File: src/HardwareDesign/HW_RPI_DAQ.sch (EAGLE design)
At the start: 348 parts, among them IC10 ADS9234RIRHBR, IC11 MCP6001RT, IC12 MCP1525T-I/TT, IC13 MCP6001RT, IC14 TPS65131, IC15 TPS7A39, IC16 SN74LVC2G66, IC17 74LVC1G04, IC2 AP22653W6, IC22 DAC8568, IC23 MCP6001RT, IC24 MCP6001RT, IC25 MCP6001RT, IC26 MCP6001RT, IC27 MCP6001RT, IC28 MCP6001RT, IC29 MCP6001RT, IC3 74LVC1G07, IC30 MCP6001RT, IC31 MCP6001RT, IC32 LSF0108, IC33 LSF0108, IC34 LSF0108, IC35 LSF0108, IC36 MCP23S18, IC38 SN74LVC2G66, IC39 74LVC1G04, IC4 RT9742NGV, IC6 DG409, IC7 ADA4254ACPZ, IC8 DG409, IC9 ADA4254ACPZ, J1 10164227-1001A1RLF, J2 10164227-1001A1RLF, J7 2-5174225-5, SW1 1825027-8, T2 IRLML5203, X2 CRYSTAL

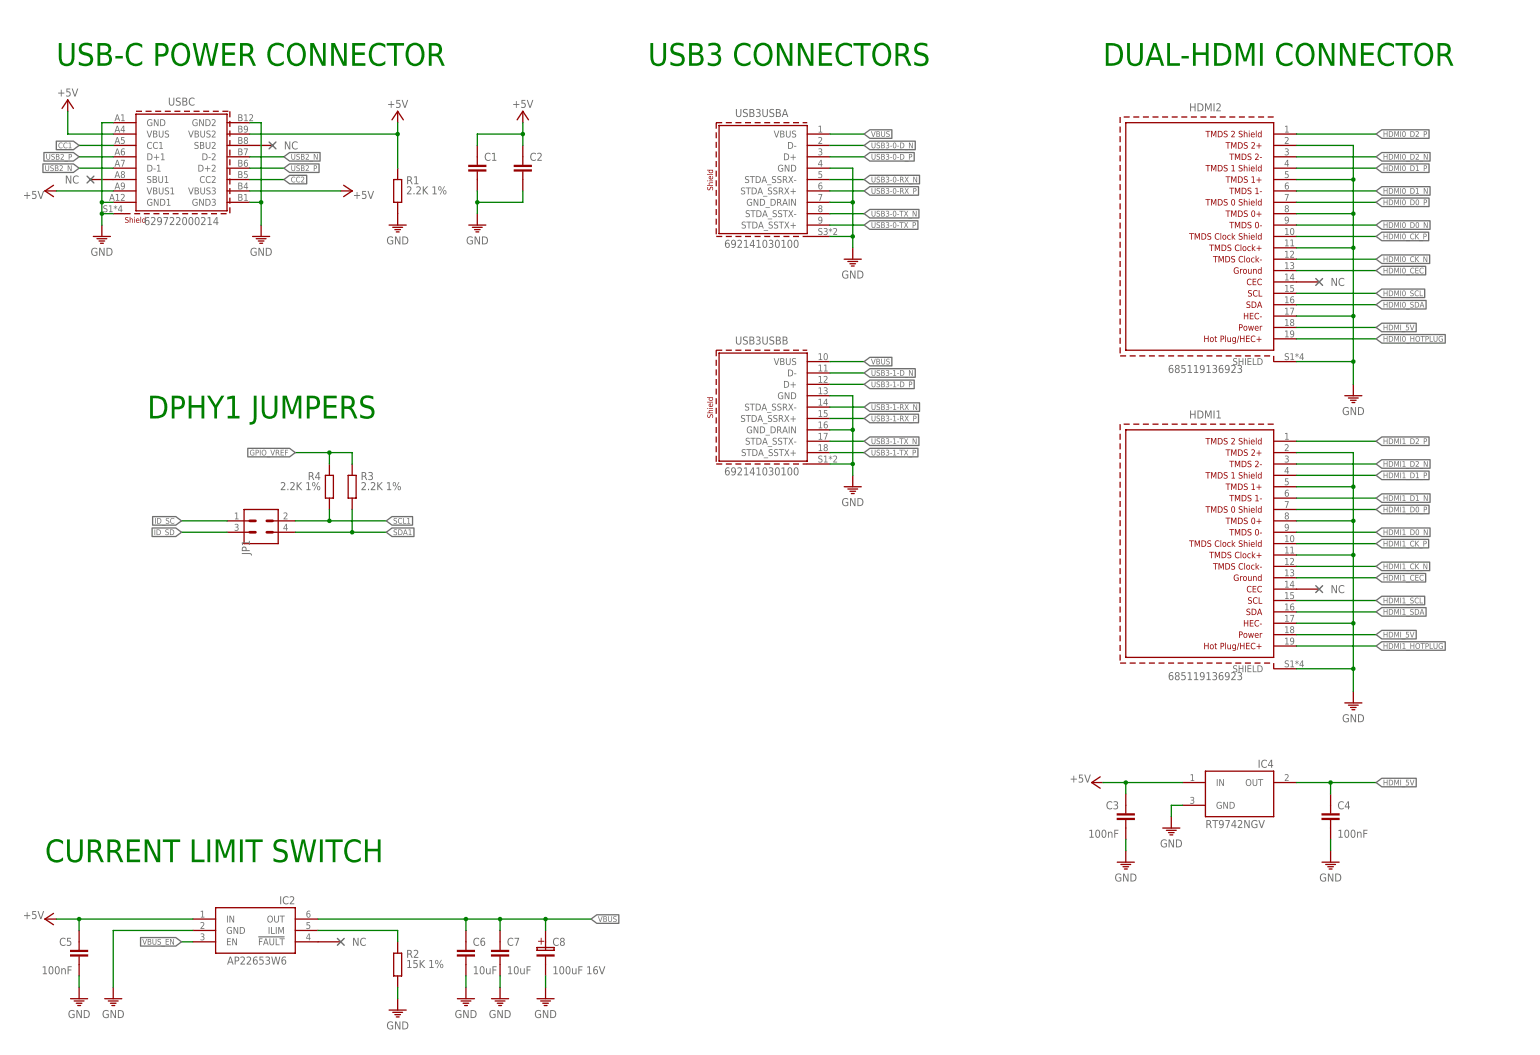
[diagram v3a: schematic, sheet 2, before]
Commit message: update schematics with new testpoints
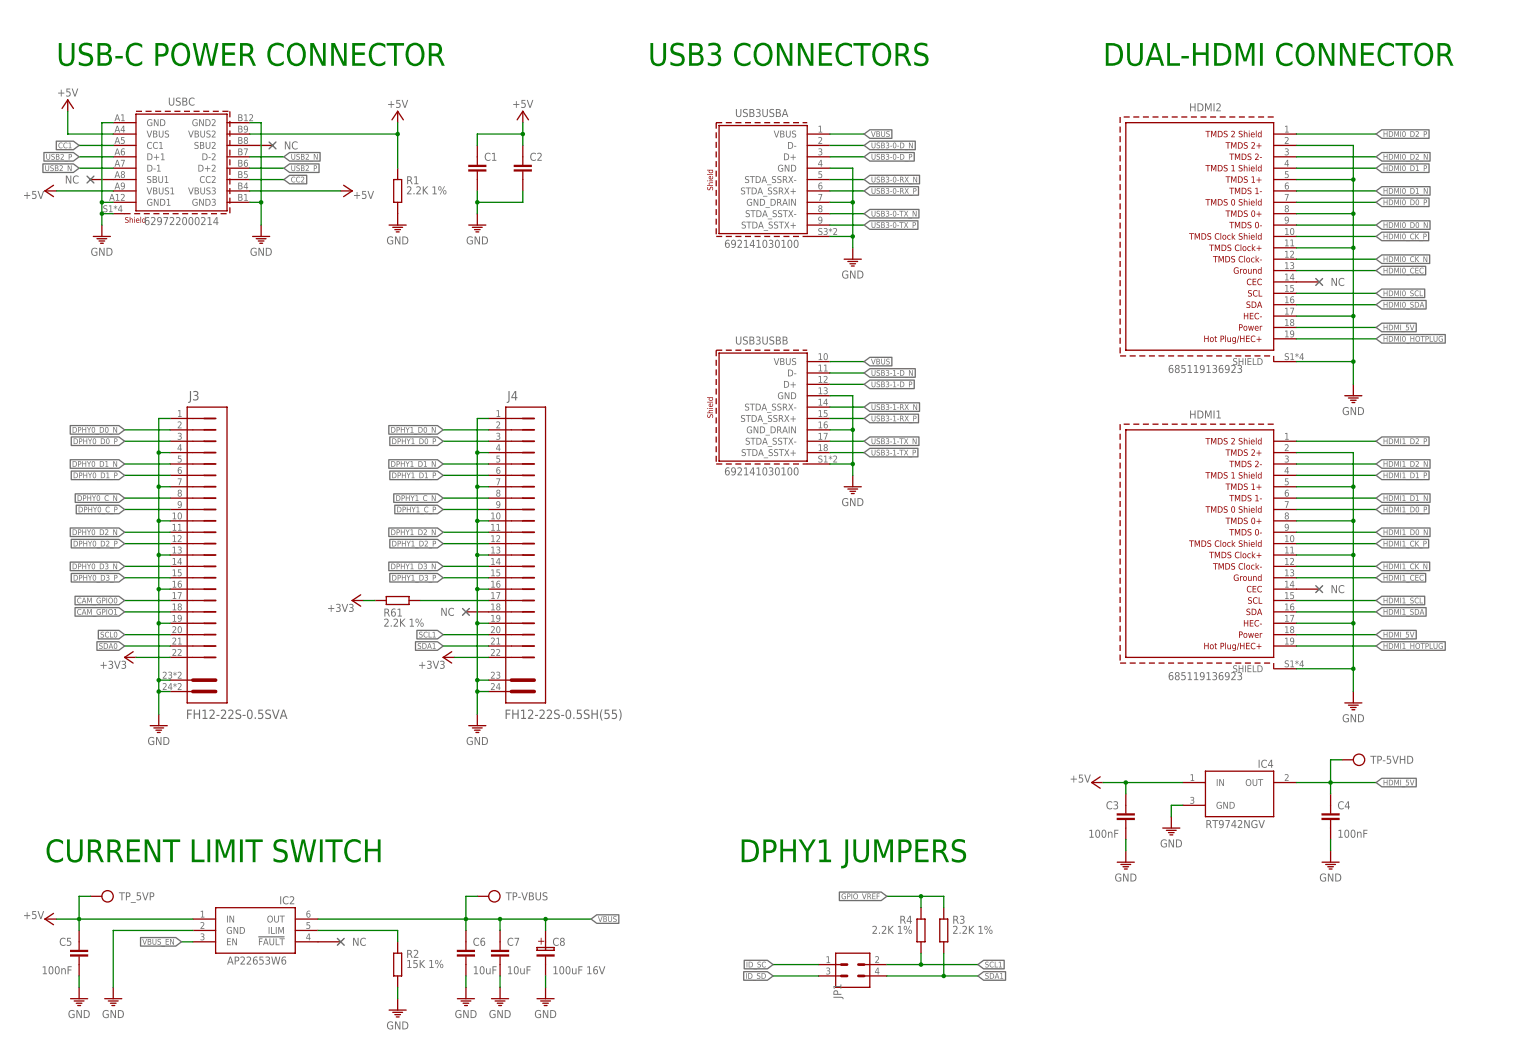
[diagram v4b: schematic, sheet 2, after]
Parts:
- added J3: FH12-22S-0.5SVA, ds_con:FH12-22S-0.5SVA
- added J4: FH12-22S-0.5SH(55), ds_con:FH12-22S-0.5SH(55)
- added R61: 2.2K 1%, ds_passive:R0402
- added TP-5VHD, TP-5VP, TP-BTN, TP-GREF, TP-LED, TP-LX, TP-M2CLK, TP-M2FB, TP-VBAT, TP-VBUS, TP-VM2, TP-VSD, TP_5VP: TP, ds_passive:TP
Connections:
- new net N$45: J4.17, R61.1
- net +3V3: now also J3.22, J4.22, R61.2
- net +5V: now also TP-5VP.P$1, TP_5VP.P$1
- net CAM_GPIO0: now also J3.17
- net CAM_GPIO1: now also J3.18
- net DPHY0_C_N: now also J3.8
- net DPHY0_C_P: now also J3.9
- net DPHY0_D0_N: now also J3.2
- net DPHY0_D0_P: now also J3.3
- net DPHY0_D1_N: now also J3.5
- net DPHY0_D1_P: now also J3.6
- net DPHY0_D2_N: now also J3.11
- net DPHY0_D2_P: now also J3.12
- net DPHY0_D3_N: now also J3.14
- net DPHY0_D3_P: now also J3.15
- net DPHY1_C_N: now also J4.8
- net DPHY1_C_P: now also J4.9
- net DPHY1_D0_N: now also J4.2
- net DPHY1_D0_P: now also J4.3
- net DPHY1_D1_N: now also J4.5
- net DPHY1_D1_P: now also J4.6
- net DPHY1_D2_N: now also J4.11
- net DPHY1_D2_P: now also J4.12
- net DPHY1_D3_N: now also J4.14
- net DPHY1_D3_P: now also J4.15
- net GND: now also J3.1, J3.10, J3.13, J3.16, J3.19, J3.4, J3.7, J3.MH1, J3.MH2, J4.1, J4.10, J4.13, J4.16, J4.19, J4.4, J4.7, J4.MH1, J4.MH2
- net GPIO_VREF: now also TP-GREF.P$1
- net HDMI_5V: now also TP-5VHD.P$1
- net M2_3V3: now also TP-VM2.P$1
- net N$10: now also TP-M2FB.P$1
- net N$11: now also TP-M2CLK.P$1
- net N$9: now also TP-LX.P$1
- net NPWR_LED: now also TP-LED.P$1
- net PWR_BUT: now also TP-BTN.P$1
- net SCL0: now also J3.20
- net SCL1: now also J4.20
- net SDA0: now also J3.21
- net SDA1: now also J4.21
- net SD_PWR: now also TP-VSD.P$1
- net VBAT: now also TP-VBAT.P$1
- net VBUS: now also TP-VBUS.P$1
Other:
- moved on the sheet: JP1, R3, R4, REF/2, REFBY2, REFOUT, SPI1_CS0, TP9, VCOMB, VOCMA, VREFR

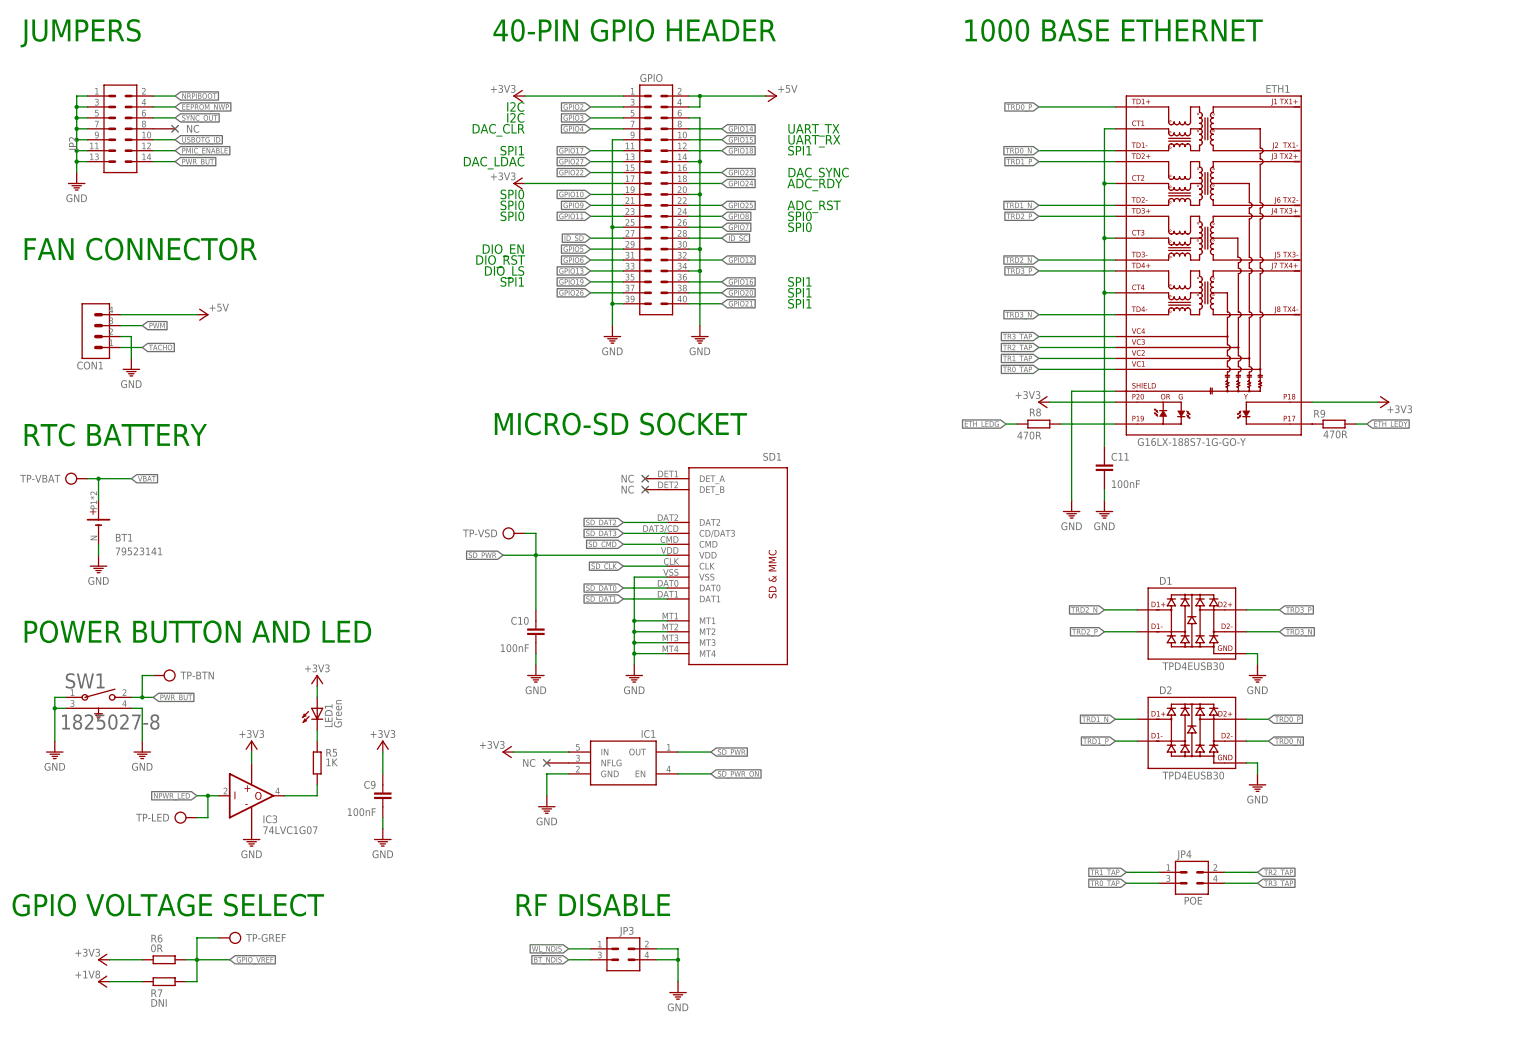
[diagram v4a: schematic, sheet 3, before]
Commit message: update PDF schematics
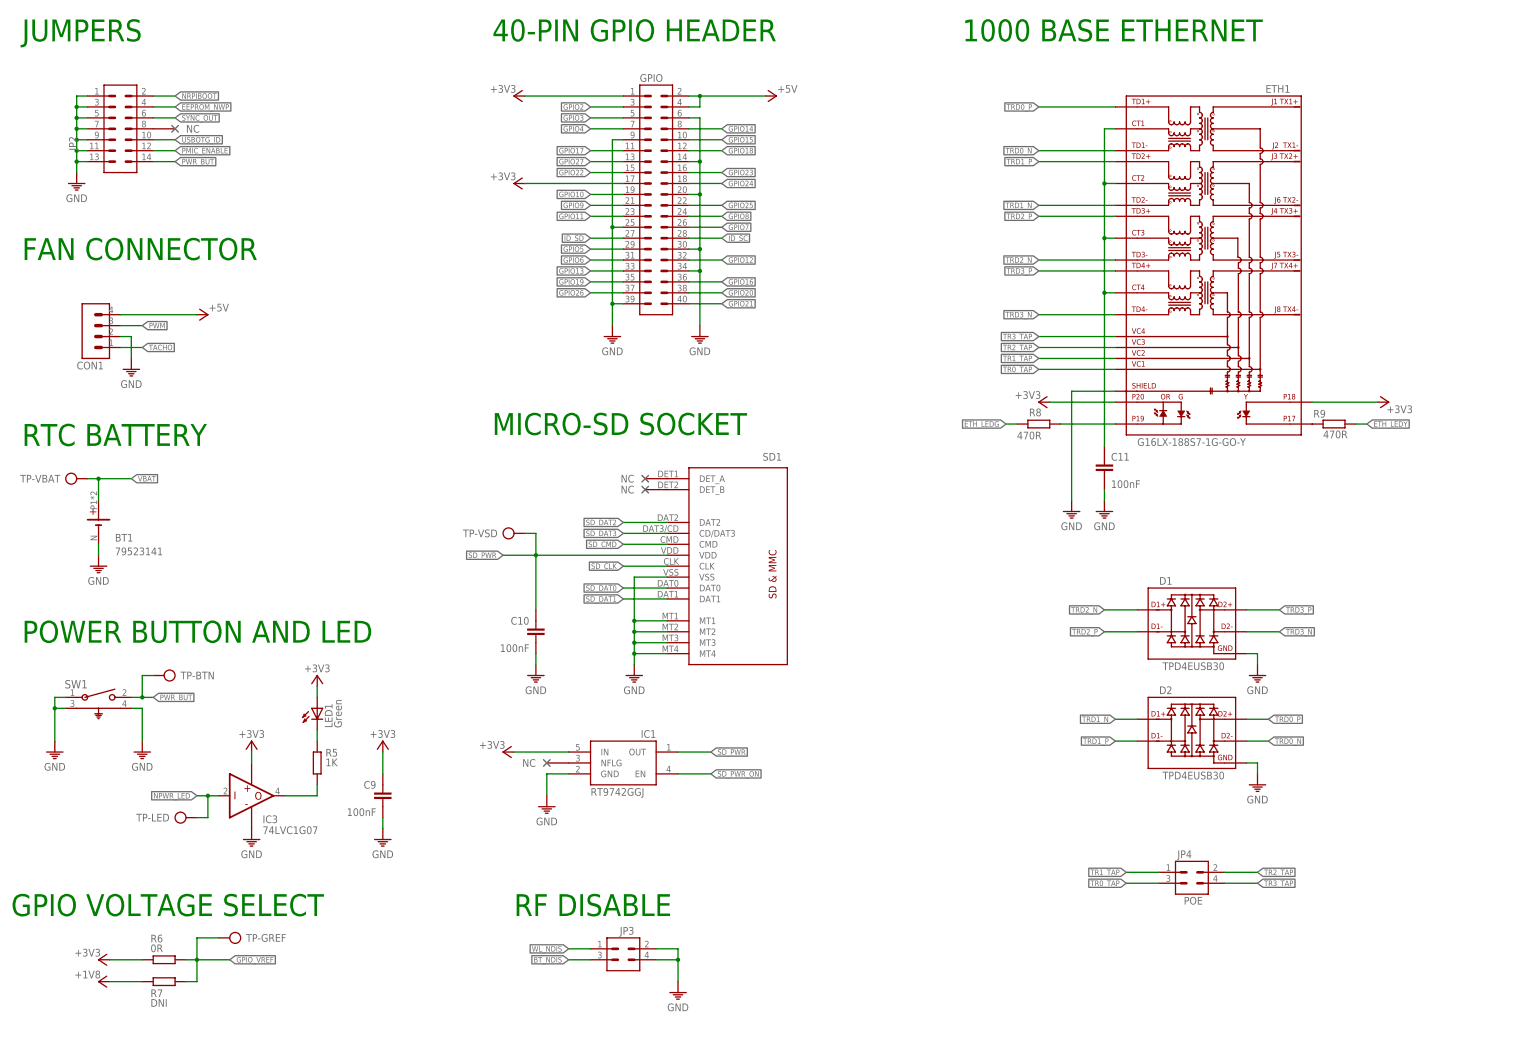
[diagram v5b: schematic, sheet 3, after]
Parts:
- IC1: value (none) -> RT9742GGJ
- IC5: value (none) -> AP3441SHE-7B
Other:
- note added: "DSI/CSI CONNECTORS"
- note removed: "ADC_RDY"
- note removed: "ADC_RST"
- note removed: "DAC_CLR"
- note removed: "DAC_LDAC"
- note removed: "DAC_SYNC"
- note removed: "DIO_EN"
- note removed: "DIO_LS"
- note removed: "DIO_RST"
- note removed: "I2C"
- note removed: "UART_RX"
- note removed: "UART_TX"
